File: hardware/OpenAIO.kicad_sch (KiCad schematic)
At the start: 4 parts, among them U24 AIO_outline, U25 INA186A3IDCKR

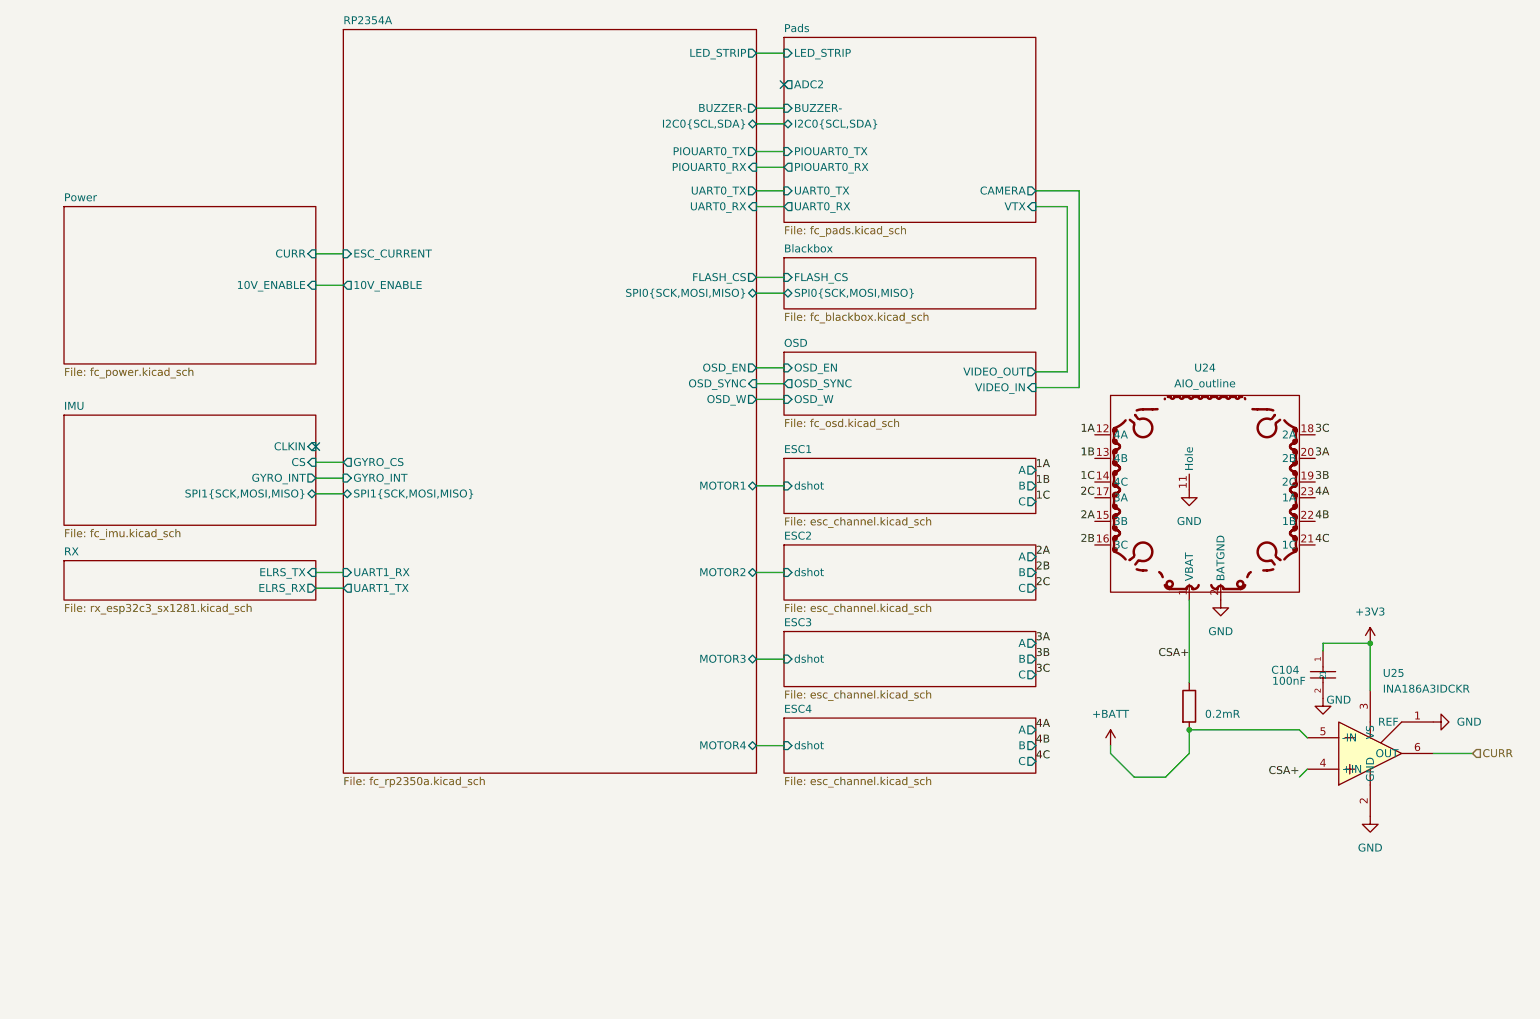
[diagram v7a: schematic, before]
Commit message: OpenAIO: two-board stack tooling, Base + Core over an interior LGA
One project, one schematic, one master PCB; the shippable boards are derived.
tools/lga_gen.py: pin table -> Core_LGA_land, Core_LGA_pads (X pre-mirrored
for B.Cu), symbol Core_LGA, core_interface sheet with global labels.
tools/lga_wire_root.py: sheet on the root, global labels on the RP2354A wires,
USB_D+/- in fc_rp2350a, root CURR hier label made global (closes the CSA link).
tools/lga_place.py: J90 on the Base, J91 flipped on the Core, paths set.
tools/split_boards.py: export/OpenAIO-Base and -Core, DRC, Core STEP as J90
3D model plus outline shadow in the master. USB netclass patterns *D+/*D-.
AGENTS.md: architecture, derived boards, layout rules.
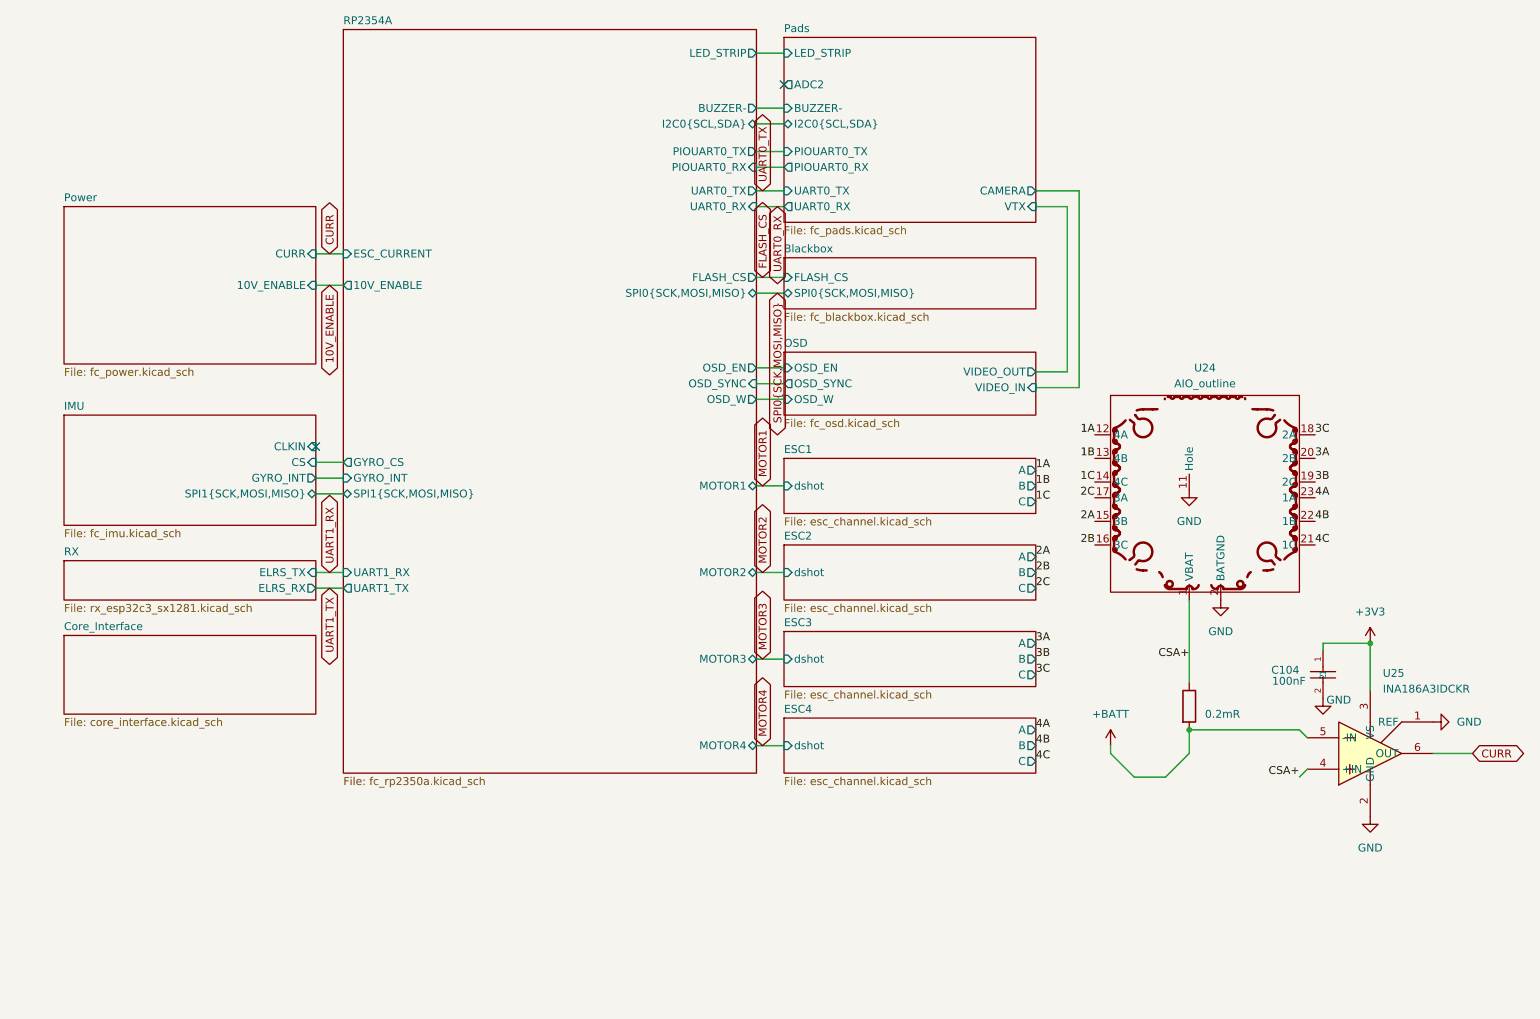
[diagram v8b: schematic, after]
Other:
- added sheet Core_Interface (core_interface.kicad_sch)
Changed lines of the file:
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@@
 		)
 	)
-	(hierarchical_label "CURR"
-		(shape input)
+	(global_label "CURR"
+		(shape bidirectional)
 		(at 260.985 137.16 0)
 		(effects
@@
 		)
 	)
+	(sheet
+		(at 33.655 118.11)
+		(size 40.64 12.7)
+		(exclude_from_sim no)
+		(in_bom yes)
+		(on_board yes)
+		(dnp no)
+		(fields_autoplaced yes)
+		(stroke
+			(width 0.1524)
+			(type solid)
+		)
+		(fill
+			(color 0 0 0 0)
+		)
+		(property "Sheetname" "Core_Interface"
+			(at 33.655 117.3984 0)
+			(show_name no)
+			(do_not_autoplace no)
+			(effects
+				(font
+					(size 1.27 1.27)
+				)
+				(justify left bottom)
+			)
+		)
+		(property "Sheetfile" "core_interface.kicad_sch"
+			(at 33.655 131.3946 0)
+			(show_name no)
+			(do_not_autoplace no)
+			(effects
+				(font
+					(size 1.27 1.27)
+				)
+				(justify left top)
+			)
+		)
+		(instances
+			(project "OpenAIO"
+				(path "/fb88b6f9-ee39-4640-a9d4-04a17ceeac64"
+					(page "13")
+				)
+			)
+		)
+	)
+	(global_label "10V_ENABLE"
+		(shape bidirectional)
+		(at 76.5175 61.595 270)
+		(effects
+			(font
+				(size 1.27 1.27)
+			)
+			(justify right)
+		)
+	)
+	(global_label "CURR"
+		(shape bidirectional)
+		(at 76.5175 56.515 90)
+		(effects
+			(font
+				(size 1.27 1.27)
+			)
+			(justify left)
+		)
+	)
+	(global_label "MOTOR1"
+		(shape bidirectional)
+		(at 146.4 93.98 90)
+		(effects
+			(font
+				(size 1.27 1.27)
+			)
+			(justify left)
+		)
+	)
+	(global_label "MOTOR2"
+		(shape bidirectional)
+		(at 146.4 107.95 90)
+		(effects
+			(font
+				(size 1.27 1.27)
+			)
+			(justify left)
+		)
+	)
+	(global_label "MOTOR3"
+		(shape bidirectional)
+		(at 146.4 121.92 90)
+		(effects
+			(font
+				(size 1.27 1.27)
+			)
+			(justify left)
+		)
+	)
+	(global_label "MOTOR4"
+		(shape bidirectional)
+		(at 146.4 135.89 90)
+		(effects
+			(font
+				(size 1.27 1.27)
+			)
+			(justify left)
+		)
+	)
+	(global_label "UART0_TX"
+		(shape bidirectional)
+		(at 146.4 46.355 90)
+		(effects
+			(font
+				(size 1.27 1.27)
+			)
+			(justify left)
+		)
+	)
+	(global_label "UART0_RX"
+		(shape bidirectional)
+		(at 148.8 48.895 270)
+		(effects
+			(font
+				(size 1.27 1.27)
+			)
+			(justify right)
+		)
+	)
+	(global_label "UART1_TX"
+		(shape bidirectional)
+		(at 76.5175 110.49 270)
+		(effects
+			(font
+				(size 1.27 1.27)
+			)
+			(justify right)
+		)
+	)
+	(global_label "UART1_RX"
+		(shape bidirectional)
+		(at 76.5175 107.95 90)
+		(effects
+			(font
+				(size 1.27 1.27)
+			)
+			(justify left)
+		)
+	)
+	(global_label "SPI0{SCK,MOSI,MISO}"
+		(shape bidirectional)
+		(at 148.8 62.865 270)
+		(effects
+			(font
+				(size 1.27 1.27)
+			)
+			(justify right)
+		)
+	)
+	(global_label "FLASH_CS"
+		(shape bidirectional)
+		(at 146.4 60.325 90)
+		(effects
+			(font
+				(size 1.27 1.27)
+			)
+			(justify left)
+		)
+	)
